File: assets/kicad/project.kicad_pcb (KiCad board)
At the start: 2 copper layers, 155.2 x 111.2 mm, 27 parts, among them J1 Adafruit microSD, J2 EPD, J3 RTC, J4 Screw_Terminal_01x03

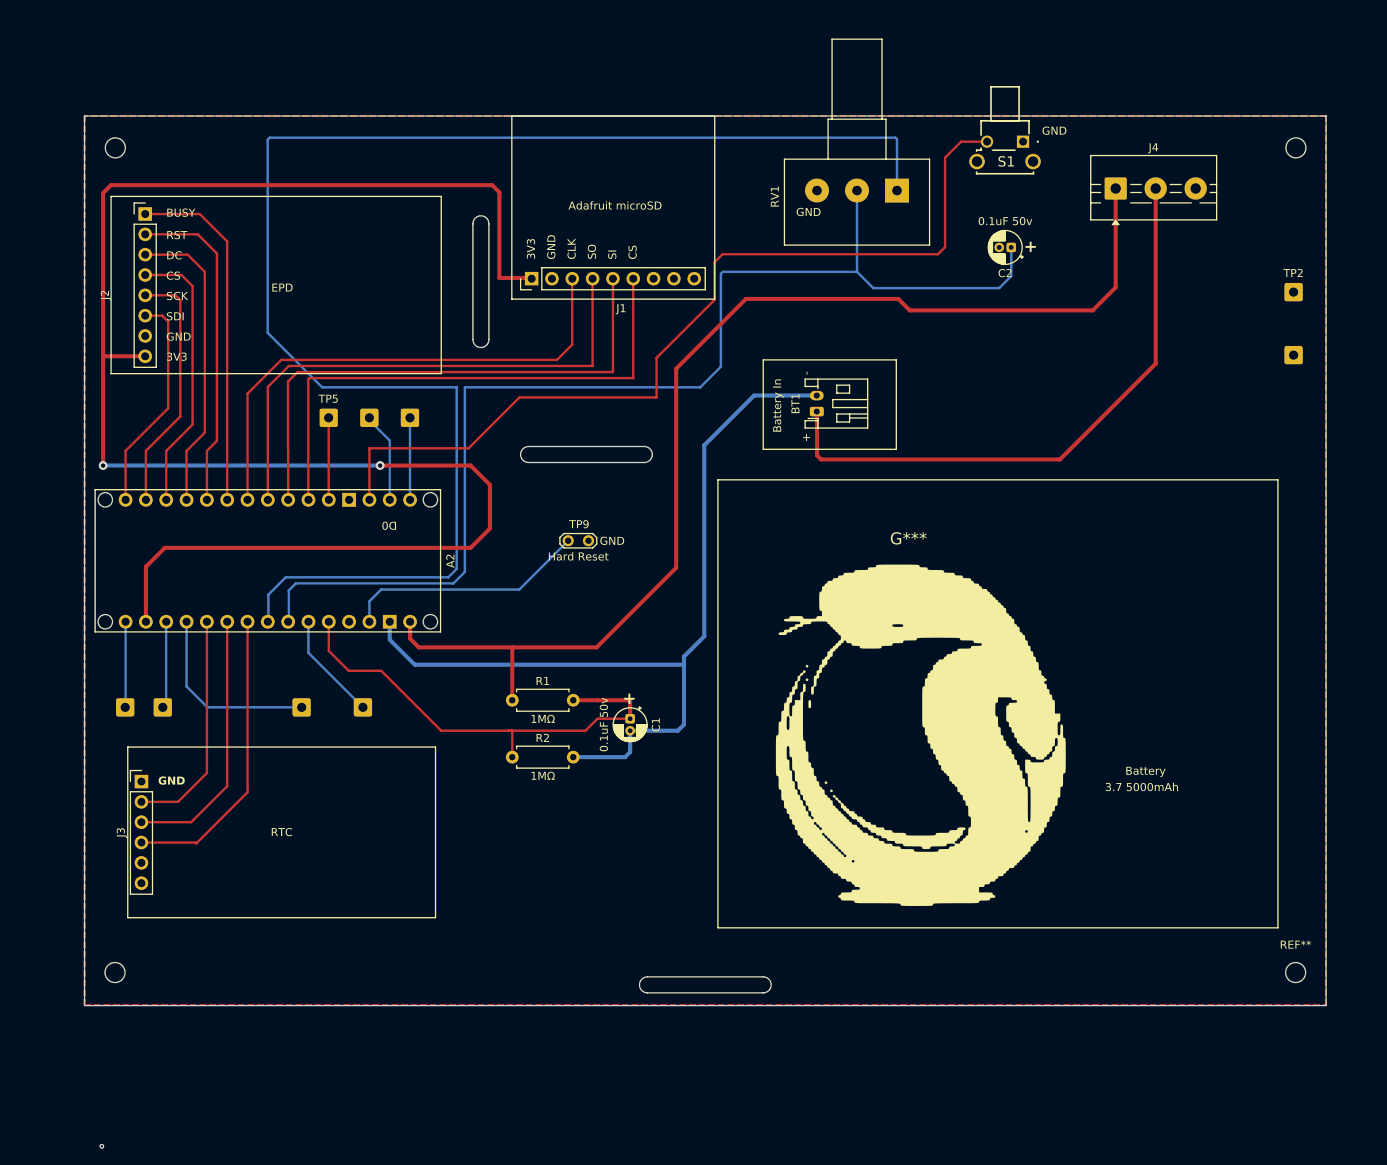
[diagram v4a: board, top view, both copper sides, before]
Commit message: toggle RTC
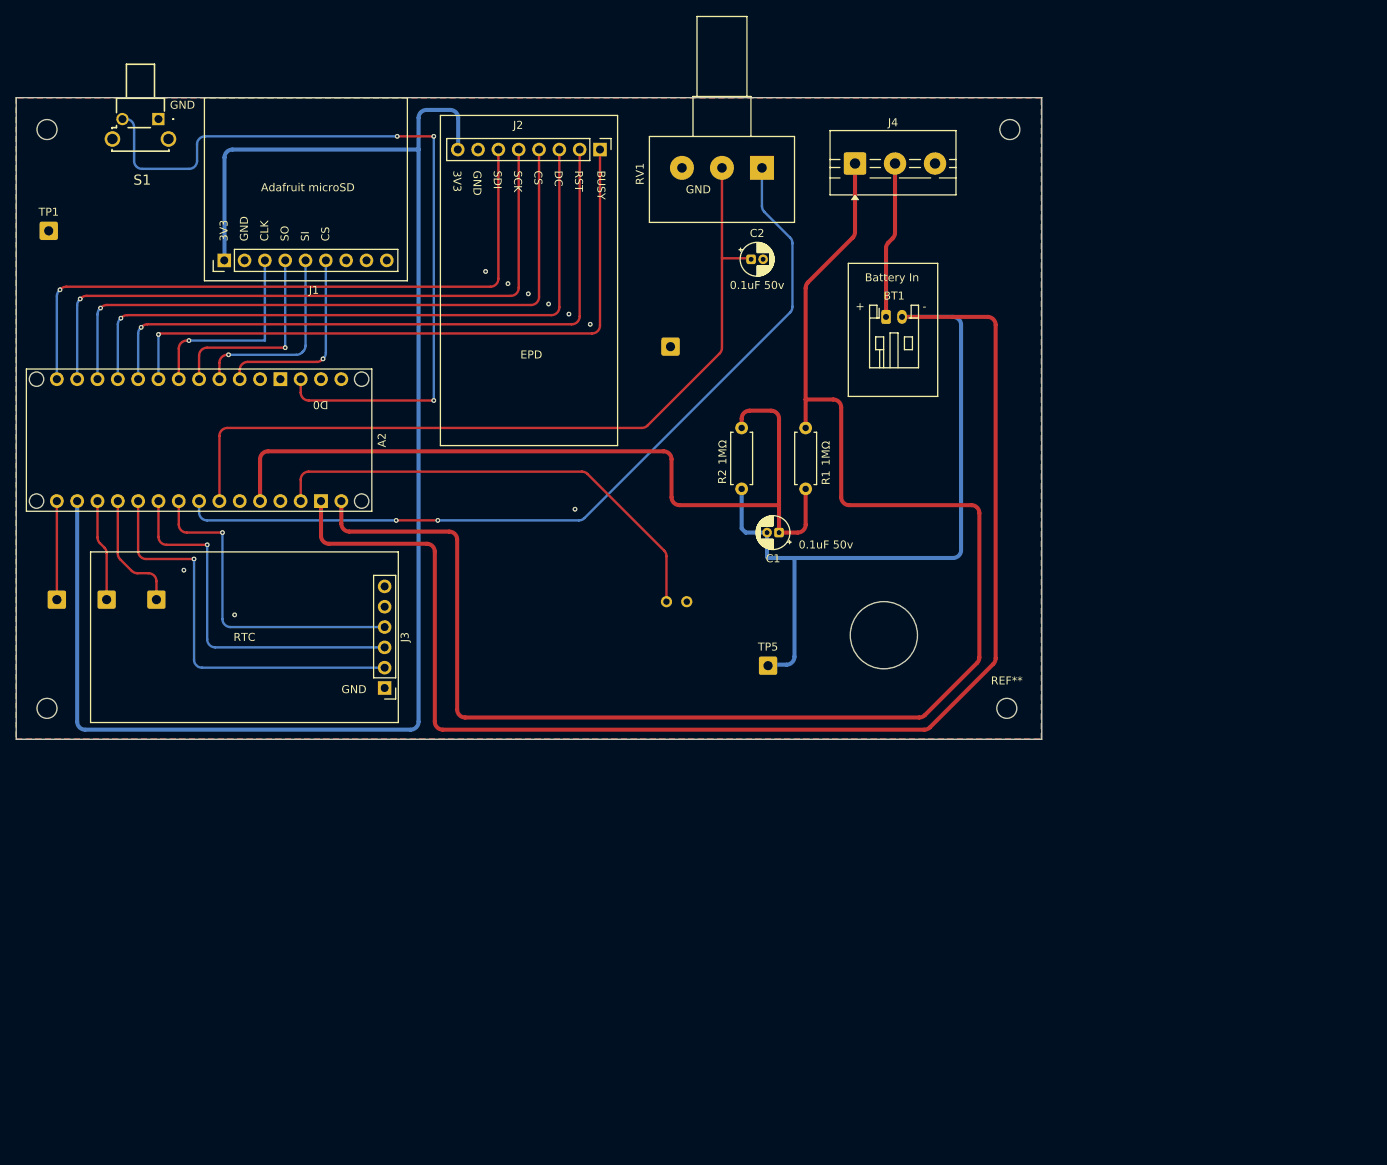
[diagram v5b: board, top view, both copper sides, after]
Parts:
- removed G***: LOGO, Sephiroth:Sepy
- removed TP6: D1/TX, Connector_Wire:SolderWire-0.5sqmm_1x01_D0.9mm_OD2.3mm
- removed TP7: D0/RX, Connector_Wire:SolderWire-0.5sqmm_1x01_D0.9mm_OD2.3mm
- removed TP8: A6, Connector_Wire:SolderWire-0.5sqmm_1x01_D0.9mm_OD2.3mm
- added REF**: MountingHole_8.4mm_M8, MountingHole:MountingHole_8.4mm_M8, F.Cu at (167.2, 114.4)
- TP1: moved to F.Cu
- TP2, TP9: moved to B.Cu
- TP5: value D2 -> GND 2
- moved TP1 156.4 mm to (62.8, 63.8), turned to 0 degrees
- moved S1 108.1 mm to (76.5, 49.9)
- moved TP2 78.2 mm to (140.5, 78.3), turned to 180 degrees
- moved TP5 63.1 mm to (152.7, 118.2)
- moved J2 57.4 mm to (131.7, 53.7), turned to -90 degrees
- moved R2 50.2 mm to (149.4, 88.5), turned to -90 degrees
- moved R1 50.0 mm to (157.4, 88.5), turned to -90 degrees
- moved REF** 48.9 mm to (182.6, 123.5)
- moved J1 38.5 mm to (84.7, 67.5)
- moved REF** 35.8 mm to (182.9, 51.2)
- moved REF** 34.1 mm to (62.6, 123.5)
- moved J4 32.7 mm to (163.6, 55.4)
- moved J3 32.6 mm to (104.8, 121.0), turned to 180 degrees
- moved C2 32.6 mm to (150.6, 67.4), turned to 0 degrees
- moved C1 29.8 mm to (154.1, 101.6), turned to 180 degrees
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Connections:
- A2 pad A6: /A6 -> unconnected-(A2-PadA6)
- A2 pad D0: /D0 -> unconnected-(A2-D0/RX-PadD0)
- A2 pad D1: /D1 -> unconnected-(A2-D1/TX-PadD1)
- A2 pad D2: /D2 -> unconnected-(A2-PadD2)
- TP5 pad 1: /D2 -> GND2
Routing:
- net GND2: track 110.7 -> 257.7 mm
- net /A4: track 186.8 -> 105.8 mm, vias 0 -> 2
- net Net-(BT1-+): track 75.0 -> 19.5 mm
- net /D12: track 27.7 -> 82.9 mm, vias 0 -> 1
- net +4V: track 144.2 -> 196.7 mm
- net /D11: track 31.4 -> 82.9 mm, vias 0 -> 1
- net /D10: track 34.6 -> 82.9 mm, vias 0 -> 1
- net /A7: track 59.3 -> 105.9 mm
- net /D9: track 37.8 -> 82.9 mm, vias 0 -> 1
- net /A5: track 146.3 -> 102.0 mm
- net /D3: track 68.2 -> 24.6 mm, vias 0 -> 1
- net /D4: track 67.6 -> 24.6 mm, vias 0 -> 1
- net /D8: track 41.3 -> 82.9 mm, vias 0 -> 1
- net /D5: track 66.7 -> 25.1 mm, vias 0 -> 1
- net /D6: track 64.7 -> 25.1 mm, vias 0 -> 1
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- removed copper zone on B.Cu, net (none)
- removed copper zone on F.Cu, net (none)
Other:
- board size 155.2 x 111.2 mm -> 128.2 x 80.2 mm
- board text added: "Photo Frame V2.0"
- board text removed: "3.7 5000mAh"
- board text removed: "Battery"
- board text removed: "Photo Frame V1.0"
